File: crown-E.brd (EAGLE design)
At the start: 57.8 x 50.8 mm, 85 parts

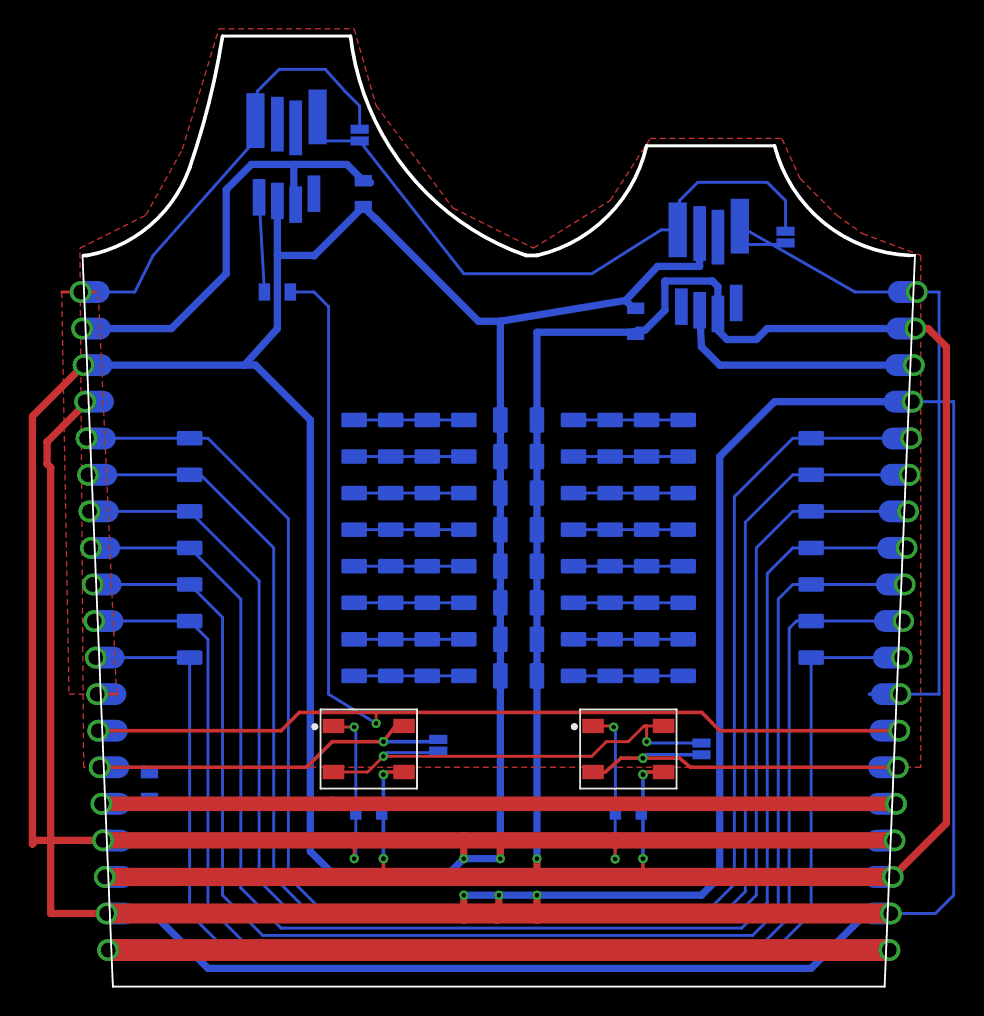
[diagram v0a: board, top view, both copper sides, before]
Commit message: Fixed stupid outline mistake on panel E
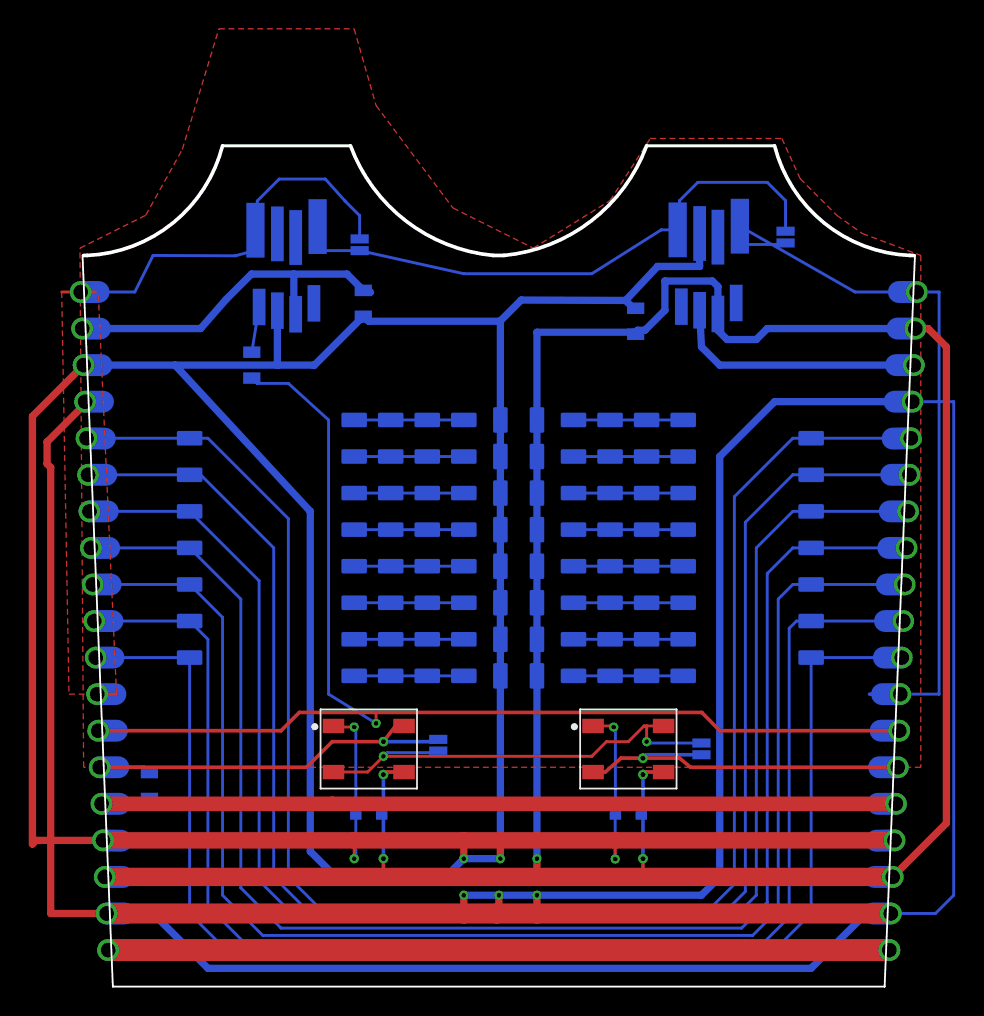
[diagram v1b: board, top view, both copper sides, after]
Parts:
- moved PTH1 7.62 mm to (14.4, 58.4)
- moved C4 7.62 mm to (19.7, 47.5)
- moved SKIP-PTH1 7.62 mm to (19.4, 51.5)
- moved PTH-END-NODE 5.38 mm to (11.9, 43.2), turned to 90 degrees
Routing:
- net VLIVE: track 289.5 -> 281.9 mm
- net N$4: track 43.8 -> 36.9 mm
- net GND: track 215.7 -> 209.2 mm
- net N$5: track 47.7 -> 43.3 mm
- net PB1: track 91.0 -> 86.9 mm
